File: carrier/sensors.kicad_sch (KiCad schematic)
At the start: 40 parts, among them J13 PWM, J14 PWM, J15 PWM, J16 PWM, J17 PWM, J18 Conn_01x10, J21 AIN, J6 Conn_01x04, J8 PWM, J9 Conn_01x04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

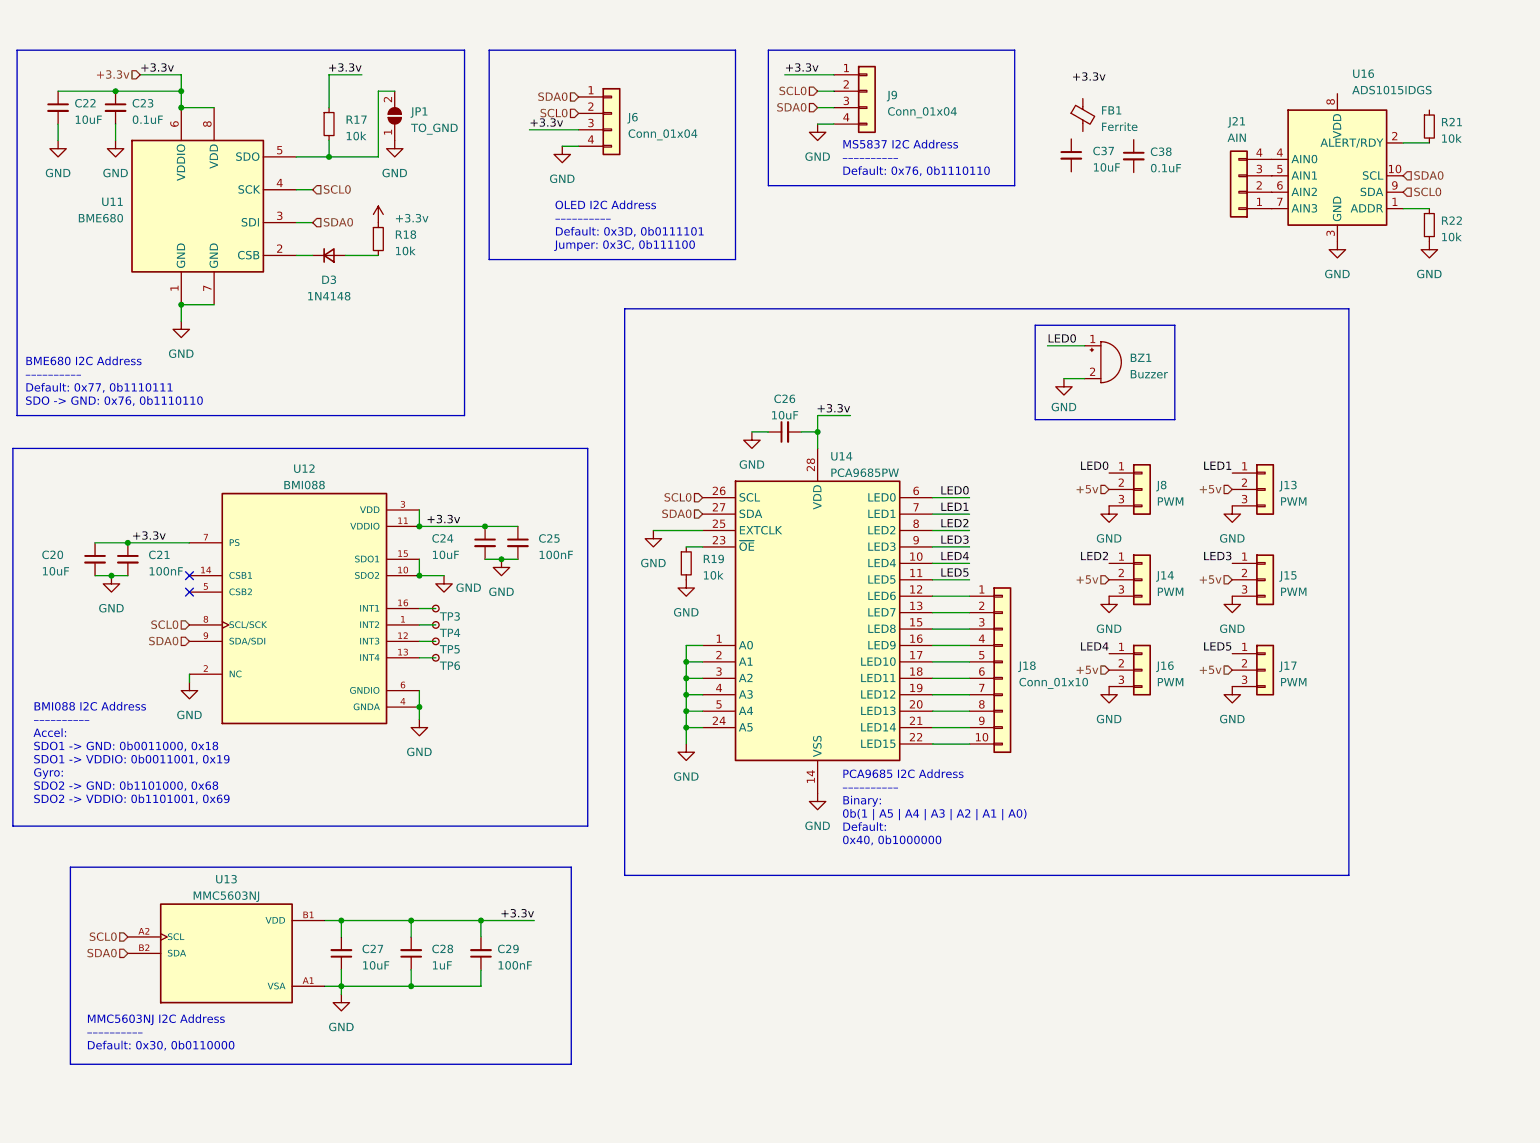
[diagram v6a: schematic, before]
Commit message: Feat: linked up majority of components to lcsc parts
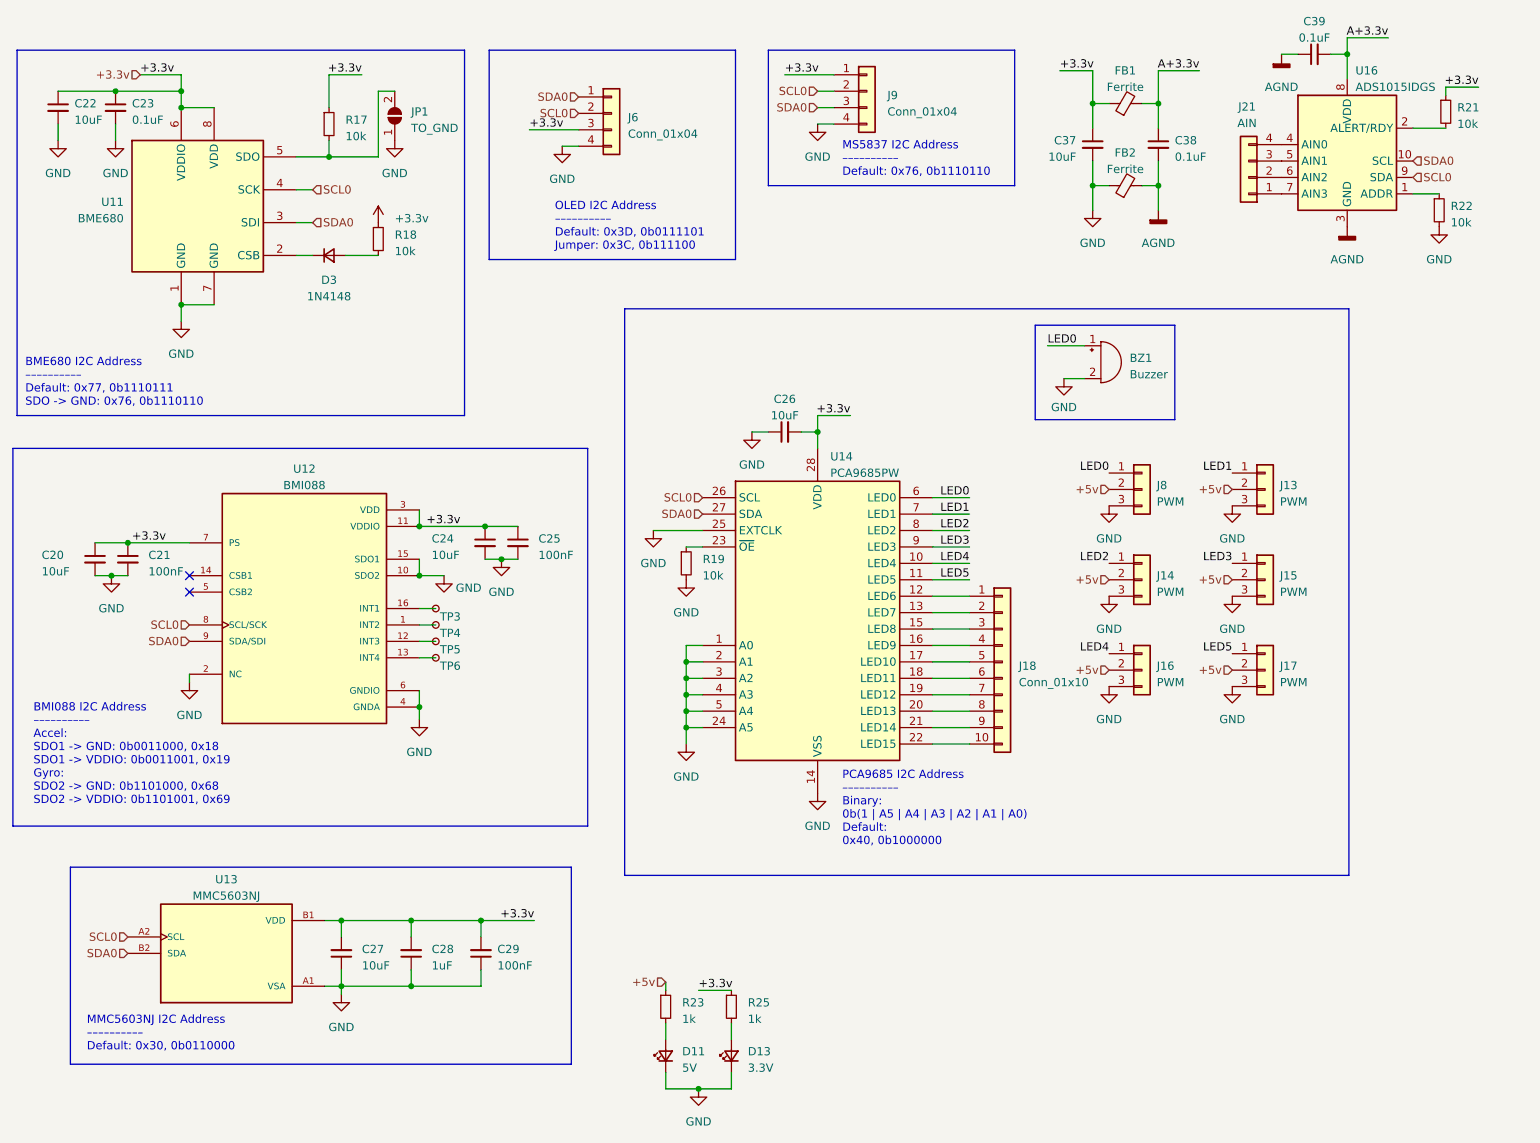
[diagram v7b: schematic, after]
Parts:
- added C39: 0.1uF, Capacitor_SMD:C_0603_1608Metric, symbol Device:C_Small
- added D11: 5V, LED_SMD:LED_0603_1608Metric, symbol Device:LED_Small
- added D13: 3.3V, LED_SMD:LED_0603_1608Metric, symbol Device:LED_Small
- added FB2: Ferrite, Inductor_SMD:L_0603_1608Metric, symbol Device:FerriteBead_Small
- added R23, R25: 1k, Resistor_SMD:R_0603_1608Metric, symbol Device:R_Small
- C37, C38: footprint (none) -> Capacitor_SMD:C_0603_1608Metric
- FB1: footprint (none) -> Inductor_SMD:L_0603_1608Metric
- R21, R22: footprint (none) -> Resistor_SMD:R_0603_1608Metric
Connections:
- net +3.3v: now also C37.1, FB1.1, R21.1, R25.1
- net +5v: now also R23.1
- net GND: now also C37.2, D11.1 (K), D13.1 (K), FB2.1; no longer U16.3 (GND)
- net A+3.3v: now reaches C38.1
- net A+3.3v: now also FB1.2, U16.8 (VDD), C39.2
- net AGND: now reaches C38.2
- net AGND: now also U16.3 (GND), C39.1, FB2.2
- new net: D13.2 (A), R25.2
- new net: D11.2 (A), R23.2
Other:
- moved on the sheet: C37, C38, FB1, J21, R21, R22, U16

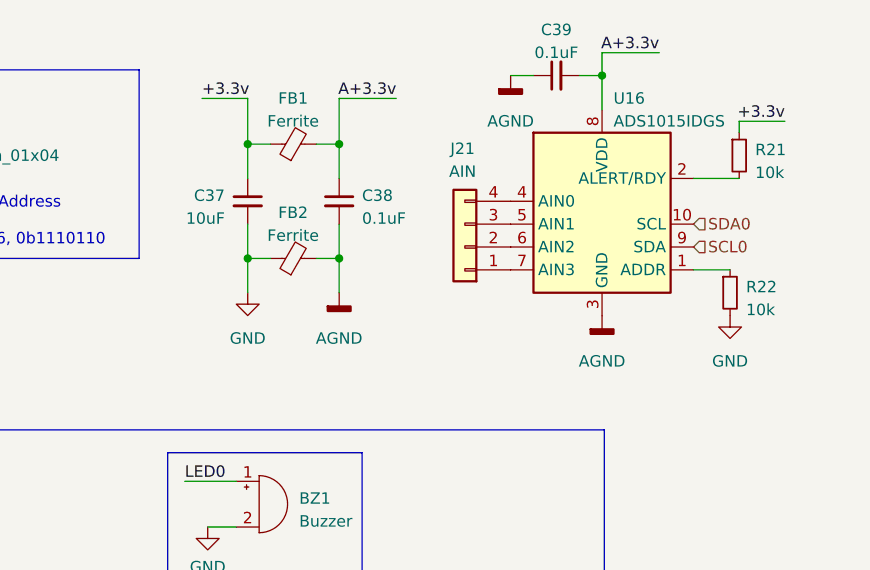
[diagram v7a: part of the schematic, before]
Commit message: Feat: restructured lower half to fit ADC + power LEDs
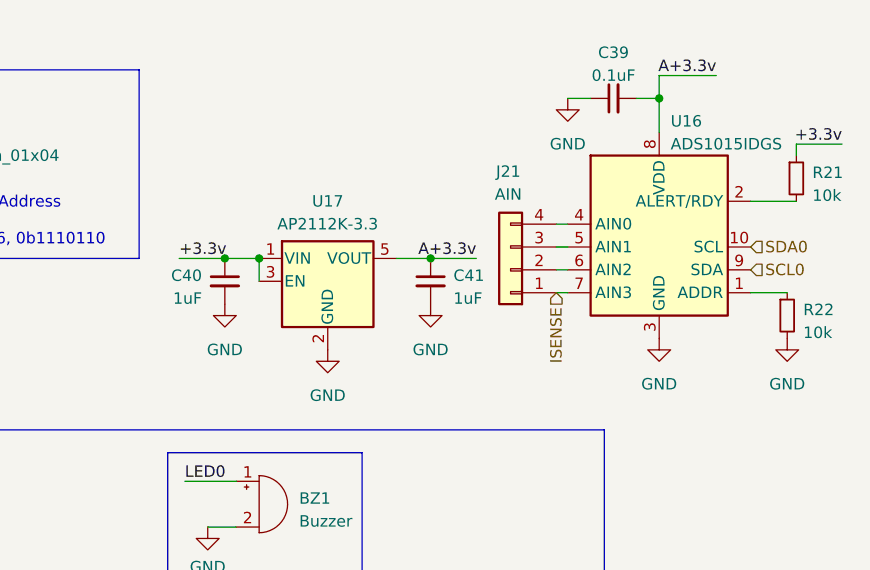
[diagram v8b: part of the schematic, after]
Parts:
- removed C37: 10uF, Capacitor_SMD:C_0603_1608Metric, symbol Device:C_Small
- removed C38: 0.1uF, Capacitor_SMD:C_0603_1608Metric, symbol Device:C_Small
- removed FB1, FB2: Ferrite, Inductor_SMD:L_0603_1608Metric, symbol Device:FerriteBead_Small
- added C40, C41: 1uF, Capacitor_SMD:C_0603_1608Metric, symbol Device:C_Small
- added U17: AP2112K-3.3, Package_TO_SOT_SMD:SOT-23-5, symbol Regulator_Linear:AP2112K-3.3
- R21, R22: footprint Resistor_SMD:R_0603_1608Metric -> Resistor_SMD:R_0402_1005Metric
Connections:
- net AGND is gone; now on net GND: C39.1, U16.3 (GND)
- net +3.3v: now also C40.1, U17.1 (VIN), U17.3 (EN)
- net A+3.3v: now also C41.1, U17.5 (VOUT)
- net GND: now also C40.2, C41.2, U17.2 (GND)
- net ISENSE: now reaches J21.1 (Pin_1), U16.7 (AIN3)
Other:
- moved on the sheet: C39, J21, R21, R22, U16
